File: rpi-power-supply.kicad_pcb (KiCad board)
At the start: 2 copper layers, 63.7 x 30 mm, 25 parts, among them IC1 ATTINY85-P, IC2 STEP_DOWN_CONVERTER_(MP2307), P1 CONN_01X03, P2 CONN_01X02, Q1 MOSFET_N_(2N7002P,215), U1 LM3480-3.3

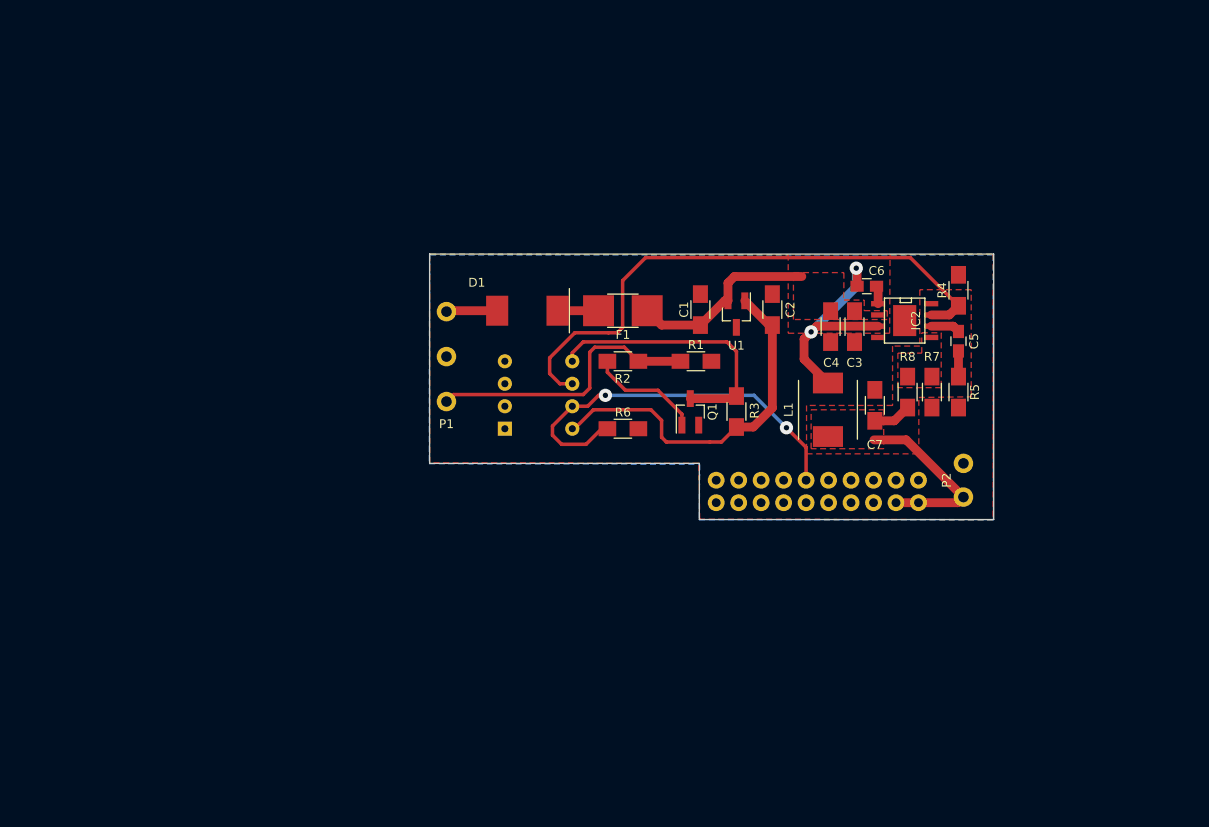
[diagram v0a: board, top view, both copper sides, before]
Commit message: - Started on PCB layout.
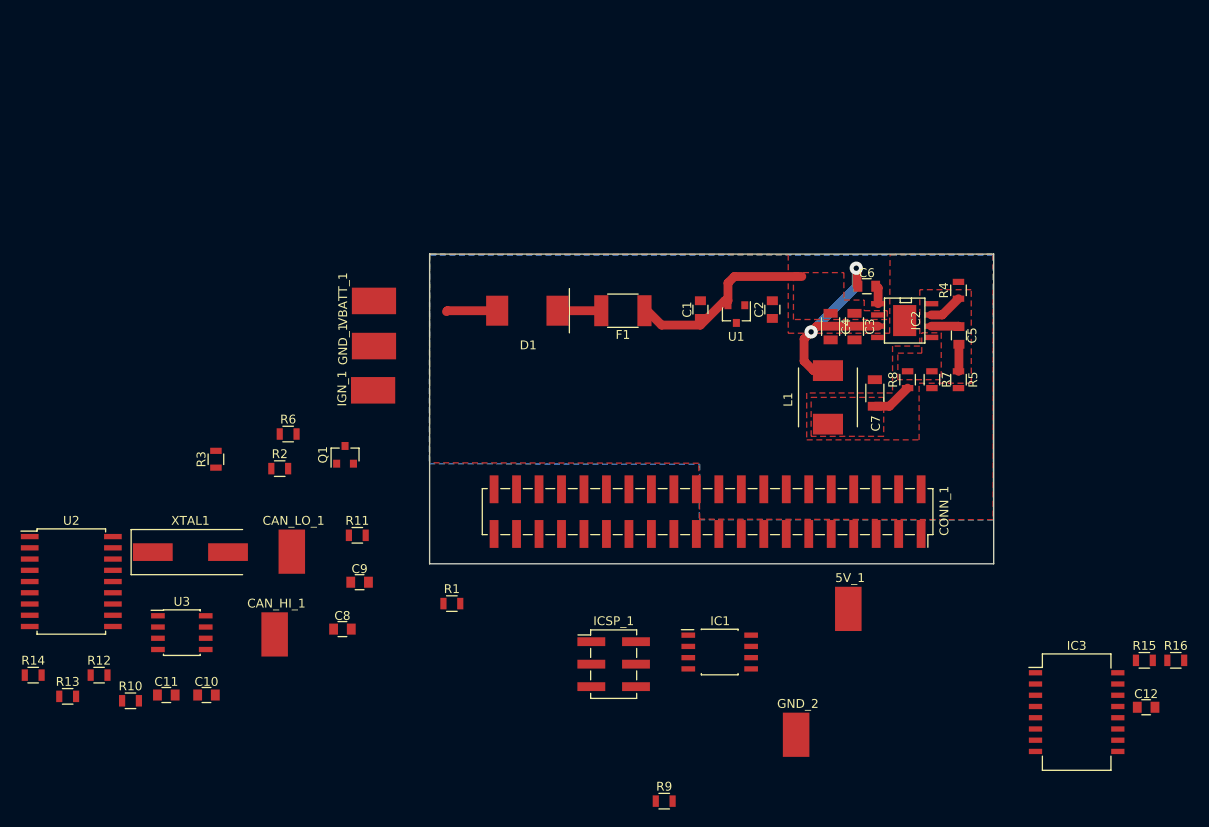
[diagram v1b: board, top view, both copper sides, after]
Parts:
- removed P1: CONN_01X03, rpi-shutdown-pcb:3_PADS_FOR_18_AWG_WIRE
- removed P2: CONN_01X02, rpi-shutdown-pcb:2_PADS_FOR_18_AWG_WIRE
- added 5V_1: CONN_01X01, rpi-power-supply:2mm_X_3mm_WIRE_PAD, F.Cu at (181.3, 139.0)
- added C10: 0.1uF, Capacitors_SMD:C_0805, F.Cu at (108.8, 148.7)
- added C11: 0.1uF, Capacitors_SMD:C_0805, F.Cu at (104.2, 148.7)
- added C12: 1uF, Capacitors_SMD:C_0805, F.Cu at (215.0, 150.1)
- added C8: 22pF, Capacitors_SMD:C_0805, F.Cu at (124.1, 141.3)
- added C9: 22pF, Capacitors_SMD:C_0805, F.Cu at (126.1, 136.0)
- added CAN_HI_1: CONN_01X01, rpi-power-supply:2mm_X_3mm_WIRE_PAD, F.Cu at (116.5, 141.9)
- added CAN_LO_1: CONN_01X01, rpi-power-supply:2mm_X_3mm_WIRE_PAD, F.Cu at (118.4, 132.5)
- added GND_1: CONN_01X01, rpi-power-supply:2mm_X_3mm_WIRE_PAD, F.Cu at (127.7, 109.3)
- added GND_2: CONN_01X01, rpi-power-supply:2mm_X_3mm_WIRE_PAD, F.Cu at (175.4, 153.2)
- added IC3: RTC_(DS3231), Housings_SOIC:SOIC-16W_7.5x12.8mm_Pitch1.27mm, F.Cu at (207.1, 150.7)
- added ICSP_1: CONN_02X03, Pin_Headers:Pin_Header_Straight_2x03_Pitch2.54mm_SMD, F.Cu at (154.8, 145.2)
- added IGN_1: CONN_01X01, rpi-power-supply:2mm_X_3mm_WIRE_PAD, F.Cu at (127.6, 114.3)
- added R10: 10K, Resistors_SMD:R_0805, F.Cu at (100.2, 149.4)
- added R11: 22K, Resistors_SMD:R_0805, F.Cu at (125.8, 130.7)
- added R12: 10K, Resistors_SMD:R_0805, F.Cu at (96.6, 146.5)
- added R13: 10K, Resistors_SMD:R_0805, F.Cu at (93.1, 148.9)
- added R14: 120R, Resistors_SMD:R_0805, F.Cu at (89.2, 146.5)
- added R15: 10K, Resistors_SMD:R_0805, F.Cu at (214.8, 144.8)
- added R16: 10K, Resistors_SMD:R_0805, F.Cu at (218.3, 144.8)
- added R9: 1K, Resistors_SMD:R_0805, F.Cu at (160.5, 160.7)
- added U2: MCP2515T-I/SO, Housings_SOIC:SOIC-18W_7.5x11.6mm_Pitch1.27mm, F.Cu at (93.5, 135.9)
- added U3: MCP2551-I/SN, Housings_SOIC:SOIC-8_3.9x4.9mm_Pitch1.27mm, F.Cu at (106.0, 141.7)
- added VBATT_1: CONN_01X01, rpi-power-supply:2mm_X_3mm_WIRE_PAD, F.Cu at (127.7, 104.2)
- added XTAL1: Crystal, Crystals:Crystal_SMD_HC49-SD, F.Cu at (107.0, 132.6)
- C1, C2: footprint rpi-shutdown-pcb:R_1206_HandSoldering_(narrow) -> Capacitors_SMD:C_0805
- C3, C4, C7: footprint rpi-shutdown-pcb:R_1206_HandSoldering_(narrow) -> Capacitors_SMD:C_1206
- C5, C6: footprint rpi-shutdown-pcb:C_0805_HandSoldering_(narrow) -> Capacitors_SMD:C_0805
- CONN_1: value CONN_02X10 -> Raspberry_Pi_2_3; footprint rpi-shutdown-pcb:HEADER_20_PIN_FEMALE_(PPTC102LFBN-RC) -> rpi-power-supply:Pin_Header_Straight_2x20_Pitch2.54mm_SMD_(mirrored); moved to F.Cu
- D1: footprint rpi-shutdown-pcb:DO-214AB -> rpi-power-supply:DO-214AB
- F1: footprint rpi-shutdown-pcb:R_1812_HandSoldering -> Resistors_SMD:R_1812
- IC1: value ATTINY85-P -> ATTINY85-20SU; footprint Housings_DIP:DIP-8_W7.62mm -> rpi-power-supply:SOIC-8_WIDE_Pitch1.27mm; moved to F.Cu
- IC2: footprint rpi-shutdown-pcb:SOIC8N_(EXPOSED_PAD) -> rpi-power-supply:SOIC8N_(EXPOSED_PAD)
- L1: footprint rpi-shutdown-pcb:INDUCTOR_10uH_(ASPI-0630LR) -> rpi-power-supply:INDUCTOR_10uH_(ASPI-0630LR)
- Q1, U1: footprint TO_SOT_Packages_SMD:SOT-23_Handsoldering -> TO_SOT_Packages_SMD:SOT-23
- R1, R2, R3, R4, R5, R6, R7, R8: footprint rpi-shutdown-pcb:R_1206_HandSoldering_(narrow) -> Resistors_SMD:R_0805
- moved R3 59.1 mm to (109.8, 122.1)
- moved R2 40.6 mm to (117.0, 123.2)
- moved Q1 39.3 mm to (124.4, 121.6)
- moved R1 38.9 mm to (136.5, 138.4)
- moved R6 37.8 mm to (118.0, 119.2)
- moved IC1 34.4 mm to (165.9, 143.9)
- moved CONN_1 24.1 mm to (165.4, 128.0), turned to 270 degrees
- moved C7 1.40 mm to (184.3, 114.6)
- moved L1 1.40 mm to (179.0, 115.1)
- moved R5 1.40 mm to (193.8, 113.1)
- moved R7 1.40 mm to (190.8, 113.1)
- moved R8 1.40 mm to (188.0, 113.1)
- moved C5 0.65 mm to (193.8, 108.1)
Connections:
- net Net-(C2-Pad1) renamed 3.3V
- net Net-(C7-Pad1) renamed 5V
- net Net-(CONN_1-Pad11) renamed SCK
- net Net-(IC1-Pad5) renamed MOSI
- net Net-(IC1-Pad6) renamed MISO
- CONN_1 pad 1: Net-(CONN_1-Pad1) -> PI_3.3V
- CONN_1 pad 17: Net-(CONN_1-Pad17) -> PI_3.3V
- CONN_1 pad 19: Net-(CONN_1-Pad19) -> PI_MOSI
- CONN_1 pad 20: Net-(CONN_1-Pad20) -> GND
- CONN_1 pad 3: Net-(CONN_1-Pad3) -> PI_SDA
- CONN_1 pad 5: Net-(CONN_1-Pad5) -> PI_SCL
- CONN_1 pad 9: Net-(CONN_1-Pad9) -> GND
- IC1 pad 1: Net-(IC1-Pad1) -> RST
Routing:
- net MISO: track 64.6 -> 3.84 mm
- net SCK: track 44.6 -> 0.00 mm, vias 2 -> 0
- net 3.3V: track 41.3 -> 0.00 mm
- net Net-(IGN_1-Pad1): track 33.1 -> 0.00 mm
- net MOSI: track 30.8 -> 0.00 mm
- net 5V: track 25.9 -> 4.55 mm
- net Net-(Q1-Pad1): track 12.9 -> 0.00 mm
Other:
- board size 63.7 x 30 mm -> 63.7 x 35 mm

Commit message: - Finished PCB design.
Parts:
- added ?: RPi_MOUNTING_HOLE, rpi-power-supply:RPi_MOUNTING_HOLE, F.Cu at (128.0, 76.3)
- added ?: RPi_MOUNTING_HOLE, rpi-power-supply:RPi_MOUNTING_HOLE, F.Cu at (186.0, 76.3)
- added ?: RPi_MOUNTING_HOLE, rpi-power-supply:RPi_MOUNTING_HOLE, F.Cu at (186.0, 125.3)
- added ?: RPi_MOUNTING_HOLE, rpi-power-supply:RPi_MOUNTING_HOLE, F.Cu at (128.0, 125.3)
- CONN_1: footprint rpi-power-supply:Pin_Header_Straight_2x20_Pitch2.54mm_SMD_(mirrored) -> rpi-power-supply:40-PIN_SMD_(M20-7812045); moved to B.Cu
- ICSP_1: footprint Pin_Headers:Pin_Header_Straight_2x03_Pitch2.54mm_SMD -> rpi-power-supply:2X3_HEADER_SMD_HORIZONTAL
- moved R10 104.6 mm to (181.2, 83.3), turned to 180 degrees
- moved C10 99.9 mm to (185.2, 84.4), turned to 90 degrees
- moved U2 95.5 mm to (177.6, 90.7)
- moved R13 92.3 mm to (166.8, 93.4)
- moved GND_2 81.2 mm to (127.1, 88.0), turned to 270 degrees
- moved R12 78.3 mm to (159.2, 99.4)
- moved 5V_1 77.1 mm to (127.1, 84.2), turned to 270 degrees
- moved C11 73.8 mm to (154.8, 95.0), turned to 90 degrees
- moved U3 71.7 mm to (160.8, 95.4)
- moved C8 70.5 mm to (165.8, 84.4)
- moved XTAL1 69.8 mm to (160.8, 88.2)
- moved R14 69.5 mm to (153.4, 120.0), turned to 90 degrees
- moved R4 61.7 mm to (134.4, 86.0), turned to 180 degrees
- moved C12 59.6 mm to (170.0, 111.0), turned to 270 degrees
- moved C9 59.5 mm to (155.8, 84.4), turned to 180 degrees
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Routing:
- net PI_3.3V: track 0.00 -> 104.3 mm, vias 0 -> 2
- net SCK: track 0.00 -> 76.9 mm, vias 0 -> 4
- net PI_SDA: track 0.00 -> 73.6 mm, vias 0 -> 1
- net 3.3V: track 0.00 -> 68.7 mm, vias 0 -> 2
- net 5V: track 4.55 -> 68.2 mm, vias 0 -> 1
- net PI_SCL: track 0.00 -> 60.5 mm, vias 0 -> 1
- net MISO: track 3.84 -> 61.0 mm, vias 0 -> 2
- net MOSI: track 0.00 -> 53.0 mm, vias 0 -> 2
- net PI_INT: track 0.00 -> 50.0 mm, vias 0 -> 1
- net Net-(CAN_HI_1-Pad1): track 0.00 -> 45.0 mm, vias 0 -> 2
- net Net-(U2-Pad1): track 0.00 -> 43.9 mm
- net PI_SS: track 0.00 -> 43.2 mm, vias 0 -> 1
- net Net-(CAN_LO_1-Pad1): track 0.00 -> 42.2 mm, vias 0 -> 2
- net PI_MOSI: track 0.00 -> 37.3 mm, vias 0 -> 1
- net PI_MISO: track 0.00 -> 31.9 mm, vias 0 -> 1
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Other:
- board size 63.7 x 35 mm -> 65.1 x 56.6 mm

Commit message: - Added connection from ignition input to RPi input.
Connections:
- CONN_1 pad 13: Net-(CONN_1-Pad13) -> MOSI
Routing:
- net MOSI: track 53.0 -> 93.2 mm, vias 2 -> 4
- net 5V: track 68.2 -> 68.9 mm
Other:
- board text added: "RPi POWER SUPPLY, v1.0 6/18"
